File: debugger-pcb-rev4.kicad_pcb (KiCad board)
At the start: 4 copper layers, 17.8 x 62.2 mm, 37 parts, among them J1 SWD-pico, J2 SWD, J3 Conn_01x21, J6 GT-USB-7010ASV, J7 Conn_01x01, J8 Conn_01x21, Q1 MMBT2222A, Q2 MMBT5401, SW1 RESET, SW2 SSSS811101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

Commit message: more progress: final overall layout
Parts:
- removed TP1: VBUS, Connector_PinHeader_2.54mm:PinHeader_1x01_P2.54mm_Vertical
- added D6: H7VL10B, Diode_SMD:D_SOD-882, F.Cu at (199.9, 105.9)
- added D7: H7VL10B, Diode_SMD:D_SOD-882, F.Cu at (199.9, 102.5)
- added J4: Conn_01x02, Connector_PinHeader_2.54mm:PinHeader_1x02_P2.54mm_Horizontal, F.Cu at (201.9, 94.0)
- D2: value SP0503BAHT -> H7VL10B; footprint Package_TO_SOT_SMD:SOT-143 -> Diode_SMD:D_SOD-882
- F1: value SMD1210-050-16V -> BSMD0805-050-24V; footprint Fuse:Fuse_1210_3225Metric -> Fuse:Fuse_0805_2012Metric
- moved R2 77.4 mm to (199.9, 107.0)
- moved R4 74.4 mm to (199.9, 103.6), turned to 180 degrees
- moved C4 74.3 mm to (200.3, 109.9)
- moved C5 72.8 mm to (200.3, 110.9)
- moved F1 65.5 mm to (199.9, 100.2), turned to 90 degrees
- moved SW3 21.1 mm to (197.6, 96.4), turned to 90 degrees
- moved SW1 15.5 mm to (190.6, 96.4)
- moved SW4 12.6 mm to (194.1, 96.4), turned to 90 degrees
- moved D2 6.55 mm to (199.9, 104.7), turned to 180 degrees
- moved J6 6.35 mm to (193.6, 104.3)
- moved SW2 5.61 mm to (203.4, 103.3)
- moved C7 0.25 mm to (200.3, 82.2)
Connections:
- F1 pad 2: Net-(D2-K-Pad4) -> Net-(D7-A2)
- J1 pad MP: (no net) -> unconnected-(J1-MountPin-PadMP)
- J6 pad A4: Net-(D2-K-Pad4) -> Net-(D7-A2)
- J6 pad A9: Net-(D2-K-Pad4) -> Net-(D7-A2)
- J6 pad B4: Net-(D2-K-Pad4) -> Net-(D7-A2)
- J6 pad B9: Net-(D2-K-Pad4) -> Net-(D7-A2)
- U1 pad 16: /USART2_TX -> /ACIA_TX
- U1 pad 17: /USART2_RX -> /ACIA_RX
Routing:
- net /USB_DM: track 0.00 -> 34.2 mm, vias 0 -> 2
- net /USB_DP: track 0.00 -> 32.1 mm, vias 0 -> 2
- net Net-(J6-CC1): track 0.00 -> 11.0 mm
- net Net-(J6-CC2): track 0.00 -> 6.57 mm
- net Net-(D7-A2): track 0.00 -> 5.74 mm
- net Net-(SW2-B): track 0.00 -> 2.56 mm
- net +5V: track 21.8 -> 23.2 mm, vias 7 -> 8
- net GND: track 23.7 -> 22.3 mm
- net /USART2_RX: track 1.36 -> 0.00 mm, vias 1 -> 0
- net /ACIA_RX: track 0.00 -> 1.36 mm, vias 0 -> 1
- added copper zone on In1.Cu, net +5V
- removed copper zone on F.Cu, net +5V
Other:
- board size 17.8 x 62.2 mm -> 17.8 x 68.6 mm
- board text added: "A1"
- board text removed: "A1.."
- board text removed: "A3"
- board text removed: "A4"
- board text removed: "A5"
- board text removed: "A6"
- board text removed: "D3"
- board text removed: "D4"
- board text removed: "D5"
- board text removed: "D6"

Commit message: close to final
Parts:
- added J5: Conn_01x02, Connector_PinHeader_2.54mm:PinHeader_1x02_P2.54mm_Vertical, F.Cu at (198.1, 53.8)
- added J9: Conn_01x02, Connector_PinHeader_2.54mm:PinHeader_1x02_P2.54mm_Vertical, F.Cu at (193.8, 90.7)
- F1: value BSMD0805-050-24V -> 0402L050SL; footprint Fuse:Fuse_0805_2012Metric -> Fuse:Fuse_0402_1005Metric
- J1: footprint Connector_JST:JST_SH_SM03B-SRSS-TB_1x03-1MP_P1.00mm_Horizontal -> custom:JST_SH_BM03B-SRSS-TB_1x03-1MP_P1.00mm_Vertical
- J4: footprint Connector_PinHeader_2.54mm:PinHeader_1x02_P2.54mm_Horizontal -> Connector_PinHeader_2.54mm:PinHeader_1x02_P2.54mm_Vertical
- Q1, Q2: footprint Package_TO_SOT_SMD:SOT-523 -> custom:SOT-523
- SW1: value RESET -> RST
- moved R9 76.1 mm to (198.3, 43.4), turned to -90 degrees
- moved R8 72.0 mm to (195.3, 43.4), turned to -90 degrees
- moved R7 71.4 mm to (196.3, 43.4), turned to 90 degrees
- moved R6 71.0 mm to (197.3, 43.4), turned to -90 degrees
- moved Q2 65.2 mm to (195.6, 45.4)
- moved Q1 65.0 mm to (198.1, 45.4)
- moved J7 54.8 mm to (196.8, 40.6), turned to 90 degrees
- moved D3 50.5 mm to (197.8, 48.2), turned to 90 degrees
- moved D4 48.9 mm to (195.8, 48.2), turned to -90 degrees
- moved J1 18.6 mm to (195.6, 61.2), turned to -90 degrees
- moved J2 14.4 mm to (200.0, 62.7), turned to 180 degrees
- moved C4 8.31 mm to (199.9, 101.6), turned to 180 degrees
- moved C5 8.31 mm to (199.9, 102.6), turned to 180 degrees
- moved D7 3.00 mm to (199.9, 99.5)
- moved J4 2.54 mm to (204.5, 94.0)
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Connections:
- J1 pad 1: /SWDIO -> /SWCLK
- J1 pad 3: /SWCLK -> /SWDIO
- J4 pad 1: /ACIA_TX -> /ACIA_RX
- J4 pad 2: /ACIA_RX -> /ACIA_TX
- U1 pad 16: /ACIA_TX -> /PA2
- U1 pad 17: /ACIA_RX -> /PA3
- U1 pad 27: unconnected-(U1-PB1-Pad27) -> /PB1
- U1 pad 33: unconnected-(U1-PB12-Pad33) -> /PB12
- U1 pad 42: /USART1_TX -> /ACIA_TX
- U1 pad 43: /USART1_RX -> /ACIA_RX
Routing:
- net Net-(U1-NRST): track 0.00 -> 29.2 mm, vias 0 -> 2
- net /PA2: track 0.00 -> 23.4 mm, vias 0 -> 1
- net Net-(U1-PB10): track 0.00 -> 21.4 mm, vias 0 -> 2
- net /PA3: track 0.00 -> 19.9 mm, vias 0 -> 2
- net Net-(U1-PB11): track 0.00 -> 19.3 mm, vias 0 -> 2
- net /ACIA_TX: track 0.00 -> 18.8 mm, vias 0 -> 1
- net /PB1: track 0.00 -> 17.6 mm, vias 0 -> 1
- net /ACIA_RX: track 1.36 -> 16.0 mm
- net /PB12: track 0.00 -> 13.8 mm, vias 0 -> 1
- net GND: track 22.3 -> 35.9 mm, vias 7 -> 15
- net /SWDIO: track 38.3 -> 25.4 mm
- net Net-(D7-A2): track 5.74 -> 15.8 mm
- net /SWCLK: track 39.9 -> 32.0 mm
- net Net-(J7-Pin_1): track 0.00 -> 5.39 mm
- net /EEPROM_~{WE}: track 30.6 -> 34.4 mm
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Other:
- outline, holes or cut-outs redrawn
- board text added: "CLK"
- board text added: "D3"
- board text added: "IO"
- board text added: "RX"
- board text added: "SWD"
- board text added: "THE PROBE!"
- board text added: "TX"

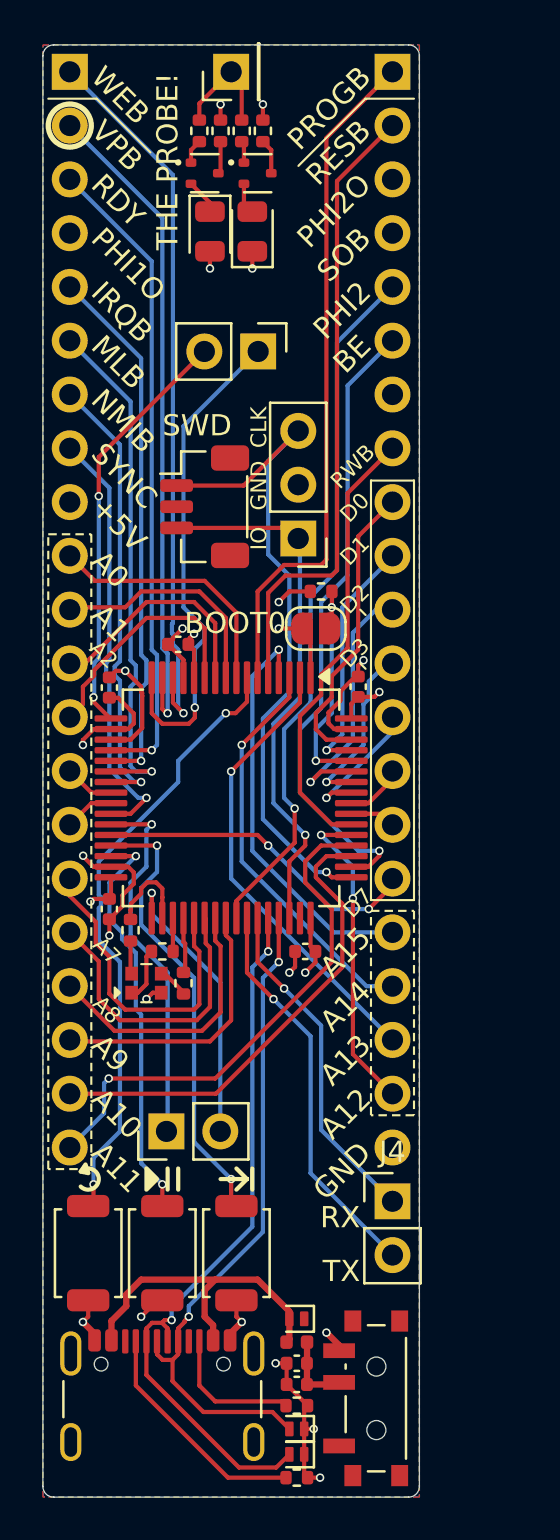
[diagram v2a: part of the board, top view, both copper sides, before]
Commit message: design reviewed and part #s added
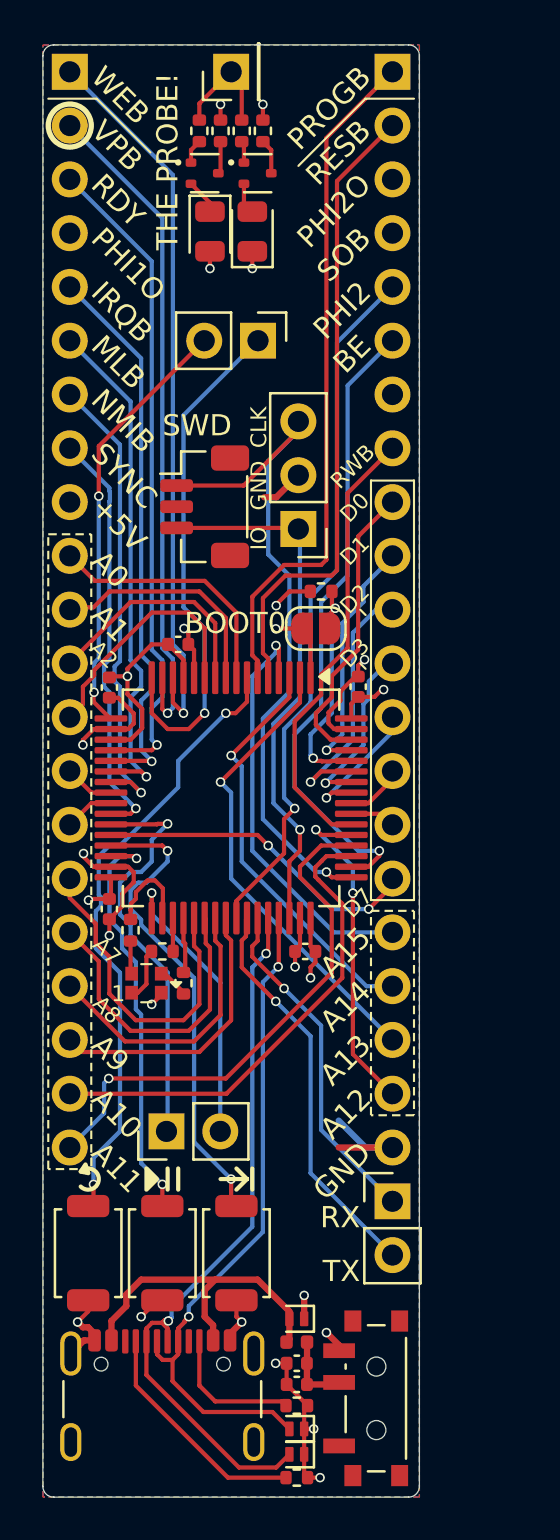
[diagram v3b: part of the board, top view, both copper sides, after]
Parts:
- D1: value R6GHBHC -> R6GHBHC-A01/2T
- R10, R5: value 470 -> 330
- R3: value 470 -> 220
- moved J5 0.51 mm to (198.1, 53.3)
- moved J2 0.45 mm to (200.0, 62.2)
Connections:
- J6 pad S1: unconnected-(J6-SHIELD-PadS1)_3 -> GND
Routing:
- net GND: track 35.9 -> 54.7 mm, vias 15 -> 16
- net +5V: track 22.7 -> 29.1 mm, vias 10 -> 9
- net /PB1: track 17.6 -> 19.4 mm
- net Net-(U1-PB10): track 21.4 -> 22.6 mm
- net /IRQB: track 25.4 -> 26.4 mm
- net /SWCLK: track 32.0 -> 32.9 mm
- net /PA2: track 23.4 -> 24.3 mm
- net /A12: track 15.0 -> 15.7 mm
- net Net-(U1-PB11): track 19.3 -> 19.8 mm
- net /SYNC: track 20.3 -> 19.8 mm
- net /NMIB: track 21.5 -> 22.0 mm
- net /PA3: track 19.9 -> 20.4 mm
- net /A11: track 24.6 -> 25.1 mm

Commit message: as ordered for batch 1
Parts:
- added G***: LOGO, custom:dergy, B.Cu at (196.6, 78.5)
- J3, J8: footprint Connector_PinHeader_2.54mm:PinHeader_1x21_P2.54mm_Vertical -> custom:PinHeader_1x21_P2.54mm_Vertical_nosilk
- moved J9 0.52 mm to (194.3, 90.8)
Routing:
- net Net-(U1-PB10): track 22.6 -> 23.2 mm
- net /USB_DM: track 34.2 -> 34.8 mm
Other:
- board text added: "A3"
- board text added: "ACIA"
- board text added: "B1"
- board text added: "B12"
- board text added: "JLCJLCJLCJLC"
- board text added: "Sky Salix"
- board text added: "by +"
- board text added: "https://breadboard.computer"
- board text added: "rev4.0"
